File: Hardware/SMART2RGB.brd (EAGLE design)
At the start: 40 x 62 mm, 11 parts, among them IC1 WS2811-SOP8, IC2 WS2811-SOP8, IC3 WS2811-SOP8, SW1 QG16F-RGB, SW2 QG16F-RGB, SW3 QG16F-RGB

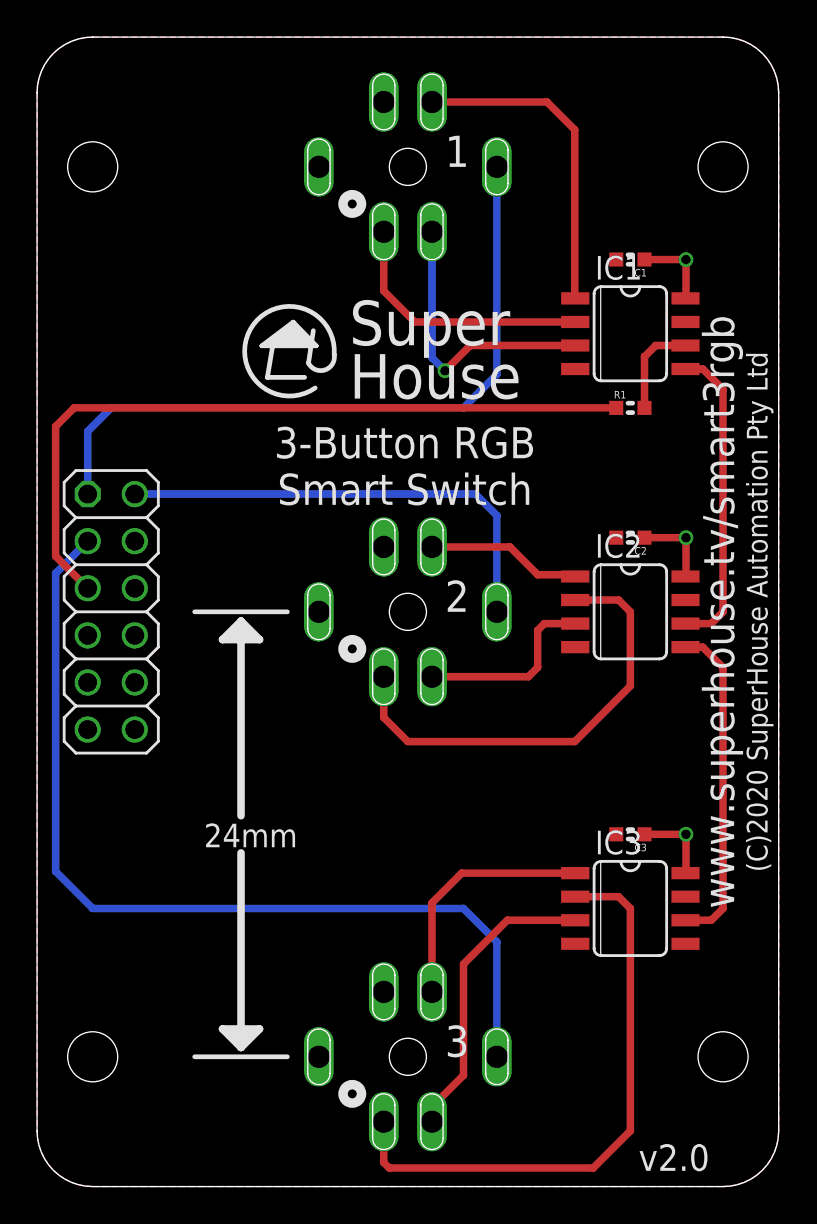
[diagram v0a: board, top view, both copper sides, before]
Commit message: Final routing, ERC, and DRC for v2.0 release.
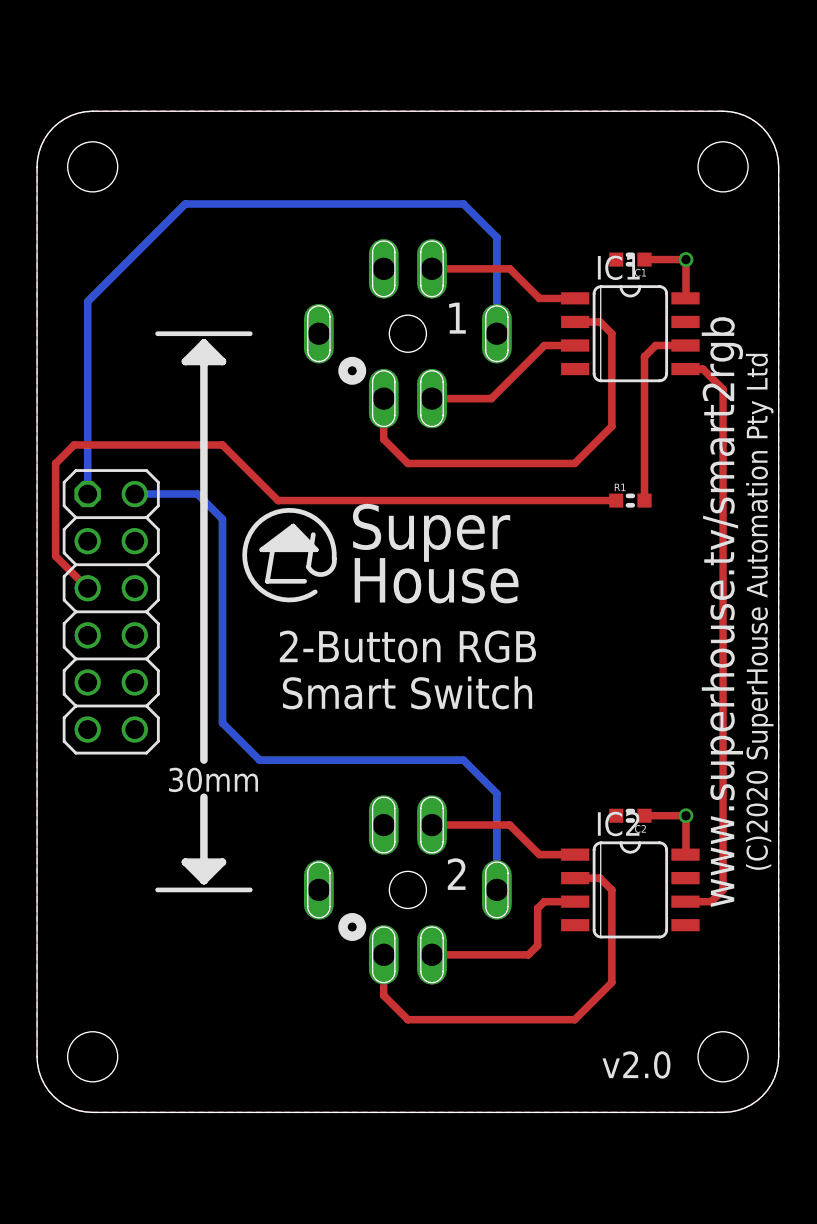
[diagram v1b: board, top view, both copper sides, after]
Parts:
- removed C3: 1uF, SuperHouse-DiscreteSemi:C0603
- removed IC3: WS2811-SOP8, SuperHouse-ICs:SO08-SKINNYPADS
- removed SW3: QG16F-RGB, SuperHouse-Switches:QG16F-RGB
- moved C2 15.0 mm to (32.0, 20.0)
- moved IC2 15.0 mm to (32.0, 16.0)
- moved SW2 15.0 mm to (20.0, 16.0)
- moved SW1 9.00 mm to (20.0, 46.0)
- moved R1 5.00 mm to (32.0, 37.0)
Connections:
- removed net LED3B: IC3.3, SW3.G
- removed net LED3G: IC3.2, SW3.B
- removed net LED3R: IC3.1, SW3.R
- removed net N$12: IC2.5, IC3.6
- net 5V: no longer C3.1, IC3.8, SW3.A
- net DATA_3: no longer SW3.1
- net GND: no longer C3.2, IC3.4, SW3.2
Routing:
- net DATA_3: track 50.1 -> 0.00 mm
- net LED3G: track 31.7 -> 0.00 mm
- net N$12: track 17.8 -> 0.00 mm
- net LED3B: track 16.2 -> 0.00 mm
- net N$6: track 16.8 -> 31.8 mm
- net LED3R: track 13.2 -> 0.00 mm
- net DATA_2: track 25.2 -> 37.9 mm
- net LED1R: track 17.4 -> 8.39 mm
- net LED1G: track 14.2 -> 23.1 mm
- net LED1B: track 15.4 -> 8.91 mm, vias 1 -> 0
- net N$1: track 5.22 -> 10.2 mm
- net 5V: track 13.0 -> 8.69 mm, vias 3 -> 2
- net DATA_1: track 37.9 -> 40.6 mm
- net LED2G: track 24.5 -> 23.1 mm
- net DATA_5: track 40.1 -> 39.3 mm
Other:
- board size 40 x 62 mm -> 40 x 54 mm
- board text added: "2-Button RGB Smart Switch"
- board text added: "30mm"
- board text added: "www.superhouse.tv/smart2rgb"
- board text removed: "24mm"
- board text removed: "3"
- board text removed: "3-Button RGB Smart Switch"
- board text removed: "www.superhouse.tv/smart3rgb"

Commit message: Converted switch isolation from FETs to diodes for v2.1 release.
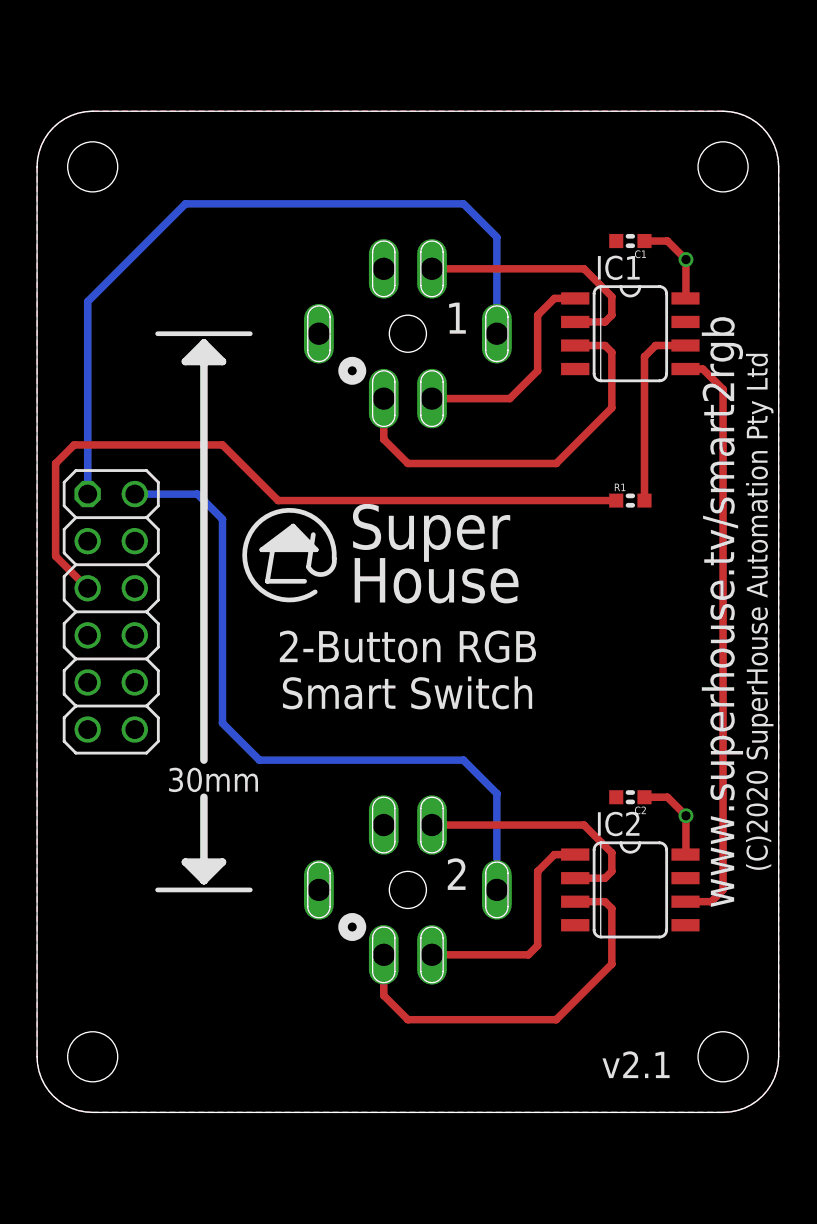
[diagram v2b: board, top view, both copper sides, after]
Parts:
- moved C1 1.00 mm to (32.0, 51.0)
- moved C2 1.00 mm to (32.0, 21.0)
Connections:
- net LED1B: now also SW1.B; no longer SW1.G
- net LED1G: now also IC1.1, SW1.G; no longer IC1.2, SW1.B
- net LED1R: now also IC1.2; no longer IC1.1
- net LED2B: now also SW2.B; no longer SW2.G
- net LED2G: now also IC2.1, SW2.G; no longer IC2.2, SW2.B
- net LED2R: now also IC2.2; no longer IC2.1
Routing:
- net LED1B: track 8.91 -> 21.4 mm
- net LED1G: track 23.1 -> 11.7 mm
- net LED2B: track 10.1 -> 21.4 mm
- net LED2G: track 23.1 -> 12.3 mm
- net LED1R: track 8.39 -> 13.4 mm
- net LED2R: track 8.39 -> 13.4 mm
- net 5V: track 8.69 -> 9.52 mm
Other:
- board text added: "v2.1"
- board text removed: "v2.0"
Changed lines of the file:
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@@
 <wire x1="40" y1="7" x2="37" y2="4" width="0" layer="20" curve="-90"/>
 <text x="39.4" y="31" size="1.1176" layer="21" font="vector" ratio="15" rot="R90" align="bottom-center">(C)2020 SuperHouse Automation Pty Ltd</text>
-<text x="30.4452" y="5.8486" size="1.4224" layer="21" font="vector" ratio="15">v2.0</text>
+<text x="30.4452" y="5.8486" size="1.4224" layer="21" font="vector" ratio="15">v2.1</text>
 <text x="20" y="27.8646" size="1.6764" layer="21" font="vector" ratio="15" align="center">2-Button RGB
 Smart Switch</text>
@@
 <attribute name="VALUE" x="29.968" y="12.063" size="1.27" layer="27" ratio="10"/>
 </element>
-<element name="C1" library="SuperHouse-DiscreteSemi" library_urn="urn:adsk.eagle:library:11768461" package="C0603" package3d_urn="urn:adsk.eagle:package:7066315/6" value="1uF" x="32" y="50" smashed="yes" rot="R180">
-<attribute name="NAME" x="32.889" y="49.492" size="0.4064" layer="25" font="vector" rot="R180"/>
-<attribute name="VALUE" x="33.016" y="50.9652" size="0.4064" layer="27" font="vector" rot="R180"/>
-</element>
-<element name="C2" library="SuperHouse-DiscreteSemi" library_urn="urn:adsk.eagle:library:11768461" package="C0603" package3d_urn="urn:adsk.eagle:package:7066315/6" value="1uF" x="32" y="20" smashed="yes" rot="R180">
-<attribute name="NAME" x="32.889" y="19.492" size="0.4064" layer="25" font="vector" rot="R180"/>
-<attribute name="VALUE" x="33.016" y="20.9652" size="0.4064" layer="27" font="vector" rot="R180"/>
+<element name="C1" library="SuperHouse-DiscreteSemi" library_urn="urn:adsk.eagle:library:11768461" package="C0603" package3d_urn="urn:adsk.eagle:package:7066315/6" value="1uF" x="32" y="51" smashed="yes" rot="R180">
+<attribute name="NAME" x="32.889" y="50.492" size="0.4064" layer="25" font="vector" rot="R180"/>
+<attribute name="VALUE" x="33.016" y="51.9652" size="0.4064" layer="27" font="vector" rot="R180"/>
+</element>
+<element name="C2" library="SuperHouse-DiscreteSemi" library_urn="urn:adsk.eagle:library:11768461" package="C0603" package3d_urn="urn:adsk.eagle:package:7066315/6" value="1uF" x="32" y="21" smashed="yes" rot="R180">
+<attribute name="NAME" x="32.889" y="20.492" size="0.4064" layer="25" font="vector" rot="R180"/>
+<attribute name="VALUE" x="33.016" y="21.9652" size="0.4064" layer="27" font="vector" rot="R180"/>
 </element>
 <element name="H1" library="SuperHouse-Connectors" library_urn="urn:adsk.eagle:library:11765989" package="2X06-S" package3d_urn="urn:adsk.eagle:package:15060598/2" value="M02X6-SOCKET" x="4" y="31" smashed="yes" rot="R270">
@@
 <via x="35" y="50" extent="1-16" drill="0.5"/>
 <via x="35" y="20" extent="1-16" drill="0.5"/>
-<wire x1="32.762" y1="50" x2="35" y2="50" width="0.4064" layer="1"/>
+<wire x1="34" y1="51" x2="32.762" y2="51" width="0.4064" layer="1"/>
+<wire x1="34" y1="51" x2="35" y2="50" width="0.4064" layer="1"/>
 <wire x1="35" y1="50" x2="35" y2="47.9316" width="0.4064" layer="1"/>
 <wire x1="35" y1="47.9316" x2="34.9734" y2="47.905" width="0.4064" layer="1"/>
-<wire x1="32.762" y1="20" x2="35" y2="20" width="0.4064" layer="1"/>
+<wire x1="34" y1="21" x2="32.762" y2="21" width="0.4064" layer="1"/>
+<wire x1="34" y1="21" x2="35" y2="20" width="0.4064" layer="1"/>
 <wire x1="35" y1="20" x2="35" y2="17.9316" width="0.4064" layer="1"/>
 <wire x1="35" y1="17.9316" x2="34.9734" y2="17.905" width="0.4064" layer="1"/>
@@
 <signal name="LED1B">
 <contactref element="IC1" pad="3"/>
-<contactref element="SW1" pad="G"/>
-<wire x1="29.0266" y1="45.365" x2="27.365" y2="45.365" width="0.4064" layer="1"/>
-<wire x1="24.5" y1="42.5" x2="21.3" y2="42.5" width="0.4064" layer="1"/>
-<wire x1="27.365" y1="45.365" x2="24.5" y2="42.5" width="0.4064" layer="1"/>
+<contactref element="SW1" pad="B"/>
+<wire x1="29.0266" y1="45.365" x2="30.635" y2="45.365" width="0.4064" layer="1"/>
+<wire x1="30.635" y1="45.365" x2="31" y2="45" width="0.4064" layer="1"/>
+<wire x1="31" y1="45" x2="31" y2="42" width="0.4064" layer="1"/>
+<wire x1="31" y1="42" x2="28" y2="39" width="0.4064" layer="1"/>
+<wire x1="28" y1="39" x2="20" y2="39" width="0.4064" layer="1"/>
+<wire x1="20" y1="39" x2="18.7" y2="40.3" width="0.4064" layer="1"/>
+<wire x1="18.7" y1="40.3" x2="18.7" y2="42.5" width="0.4064" layer="1"/>
 </signal>
 <signal name="LED2B">
 <contactref element="IC2" pad="3"/>
-<contactref element="SW2" pad="G"/>
-<wire x1="29.0266" y1="15.365" x2="27.365" y2="15.365" width="0.4064" layer="1"/>
-<wire x1="27.365" y1="15.365" x2="27" y2="15" width="0.4064" layer="1"/>
-<wire x1="27" y1="15" x2="27" y2="13" width="0.4064" layer="1"/>
-<wire x1="27" y1="13" x2="26.5" y2="12.5" width="0.4064" layer="1"/>
-<wire x1="26.5" y1="12.5" x2="21.3" y2="12.5" width="0.4064" layer="1"/>
+<contactref element="SW2" pad="B"/>
+<wire x1="29.0266" y1="15.365" x2="30.635" y2="15.365" width="0.4064" layer="1"/>
+<wire x1="30.635" y1="15.365" x2="31" y2="15" width="0.4064" layer="1"/>
+<wire x1="31" y1="15" x2="31" y2="12" width="0.4064" layer="1"/>
+<wire x1="28" y1="9" x2="20" y2="9" width="0.4064" layer="1"/>
+<wire x1="20" y1="9" x2="18.7" y2="10.3" width="0.4064" layer="1"/>
+<wire x1="18.7" y1="10.3" x2="18.7" y2="12.5" width="0.4064" layer="1"/>
+<wire x1="31" y1="12" x2="28" y2="9" width="0.4064" layer="1"/>
 </signal>
 <signal name="N$6">
@@
 <signal name="LED1R">
 <contactref element="SW1" pad="R"/>
+<contactref element="IC1" pad="2"/>
+<wire x1="29.0266" y1="46.635" x2="30.635" y2="46.635" width="0.4064" layer="1"/>
+<wire x1="30.635" y1="46.635" x2="31" y2="47" width="0.4064" layer="1"/>
+<wire x1="31" y1="47" x2="31" y2="48" width="0.4064" layer="1"/>
+<wire x1="31" y1="48" x2="29.5" y2="49.5" width="0.4064" layer="1"/>
+<wire x1="29.5" y1="49.5" x2="21.3" y2="49.5" width="0.4064" layer="1"/>
+</signal>
+<signal name="LED1G">
+<contactref element="SW1" pad="G"/>
 <contactref element="IC1" pad="1"/>
-<wire x1="21.3" y1="49.5" x2="25.5" y2="49.5" width="0.4064" layer="1"/>
-<wire x1="27.095" y1="47.905" x2="29.0266" y2="47.905" width="0.4064" layer="1"/>
-<wire x1="25.5" y1="49.5" x2="27.095" y2="47.905" width="0.4064" layer="1"/>
-</signal>
-<signal name="LED1G">
-<contactref element="IC1" pad="2"/>
-<contactref element="SW1" pad="B"/>
-<wire x1="29.0266" y1="46.635" x2="30.365" y2="46.635" width="0.4064" layer="1"/>
-<wire x1="30.365" y1="46.635" x2="31" y2="46" width="0.4064" layer="1"/>
-<wire x1="20" y1="39" x2="18.7" y2="40.3" width="0.4064" layer="1"/>
-<wire x1="18.7" y1="40.3" x2="18.7" y2="42.5" width="0.4064" layer="1"/>
-<wire x1="31" y1="46" x2="31" y2="41" width="0.4064" layer="1"/>
-<wire x1="31" y1="41" x2="29" y2="39" width="0.4064" layer="1"/>
-<wire x1="29" y1="39" x2="20" y2="39" width="0.4064" layer="1"/>
+<wire x1="29.0266" y1="47.905" x2="27.905" y2="47.905" width="0.4064" layer="1"/>
+<wire x1="27.905" y1="47.905" x2="27" y2="47" width="0.4064" layer="1"/>
+<wire x1="27" y1="47" x2="27" y2="44" width="0.4064" layer="1"/>
+<wire x1="27" y1="44" x2="25.5" y2="42.5" width="0.4064" layer="1"/>
+<wire x1="25.5" y1="42.5" x2="21.3" y2="42.5" width="0.4064" layer="1"/>
 </signal>
 <signal name="LED2G">
-<contactref element="IC2" pad="2"/>
-<contactref element="SW2" pad="B"/>
-<wire x1="29.0266" y1="16.635" x2="30.365" y2="16.635" width="0.4064" layer="1"/>
-<wire x1="30.365" y1="16.635" x2="31" y2="16" width="0.4064" layer="1"/>
-<wire x1="31" y1="16" x2="31" y2="11" width="0.4064" layer="1"/>
-<wire x1="31" y1="11" x2="29" y2="9" width="0.4064" layer="1"/>
-<wire x1="20" y1="9" x2="18.7" y2="10.3" width="0.4064" layer="1"/>
-<wire x1="18.7" y1="10.3" x2="18.7" y2="12.5" width="0.4064" layer="1"/>
-<wire x1="29" y1="9" x2="20" y2="9" width="0.4064" layer="1"/>
+<contactref element="SW2" pad="G"/>
+<contactref element="IC2" pad="1"/>
+<wire x1="29.0266" y1="17.905" x2="27.905" y2="17.905" width="0.4064" layer="1"/>
+<wire x1="27.905" y1="17.905" x2="27" y2="17" width="0.4064" layer="1"/>
+<wire x1="27" y1="17" x2="27" y2="13" width="0.4064" layer="1"/>
+<wire x1="27" y1="13" x2="26.5" y2="12.5" width="0.4064" layer="1"/>
+<wire x1="26.5" y1="12.5" x2="21.3" y2="12.5" width="0.4064" layer="1"/>
 </signal>
 <signal name="LED2R">
 <contactref element="SW2" pad="R"/>
-<contactref element="IC2" pad="1"/>
-<wire x1="21.3" y1="19.5" x2="25.5" y2="19.5" width="0.4064" layer="1"/>
-<wire x1="27.095" y1="17.905" x2="29.0266" y2="17.905" width="0.4064" layer="1"/>
-<wire x1="25.5" y1="19.5" x2="27.095" y2="17.905" width="0.4064" layer="1"/>
+<contactref element="IC2" pad="2"/>
+<wire x1="29.0266" y1="16.635" x2="30.635" y2="16.635" width="0.4064" layer="1"/>
+<wire x1="30.635" y1="16.635" x2="31" y2="17" width="0.4064" layer="1"/>
+<wire x1="31" y1="17" x2="31" y2="18" width="0.4064" layer="1"/>
+<wire x1="31" y1="18" x2="29.5" y2="19.5" width="0.4064" layer="1"/>
+<wire x1="29.5" y1="19.5" x2="21.3" y2="19.5" width="0.4064" layer="1"/>
 </signal>
 </signals>
